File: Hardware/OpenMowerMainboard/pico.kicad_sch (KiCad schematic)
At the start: 7 parts, among them U10 74HC4051, U11 Pico, U7 SN74LV1T34DBV, U9 74HC4051

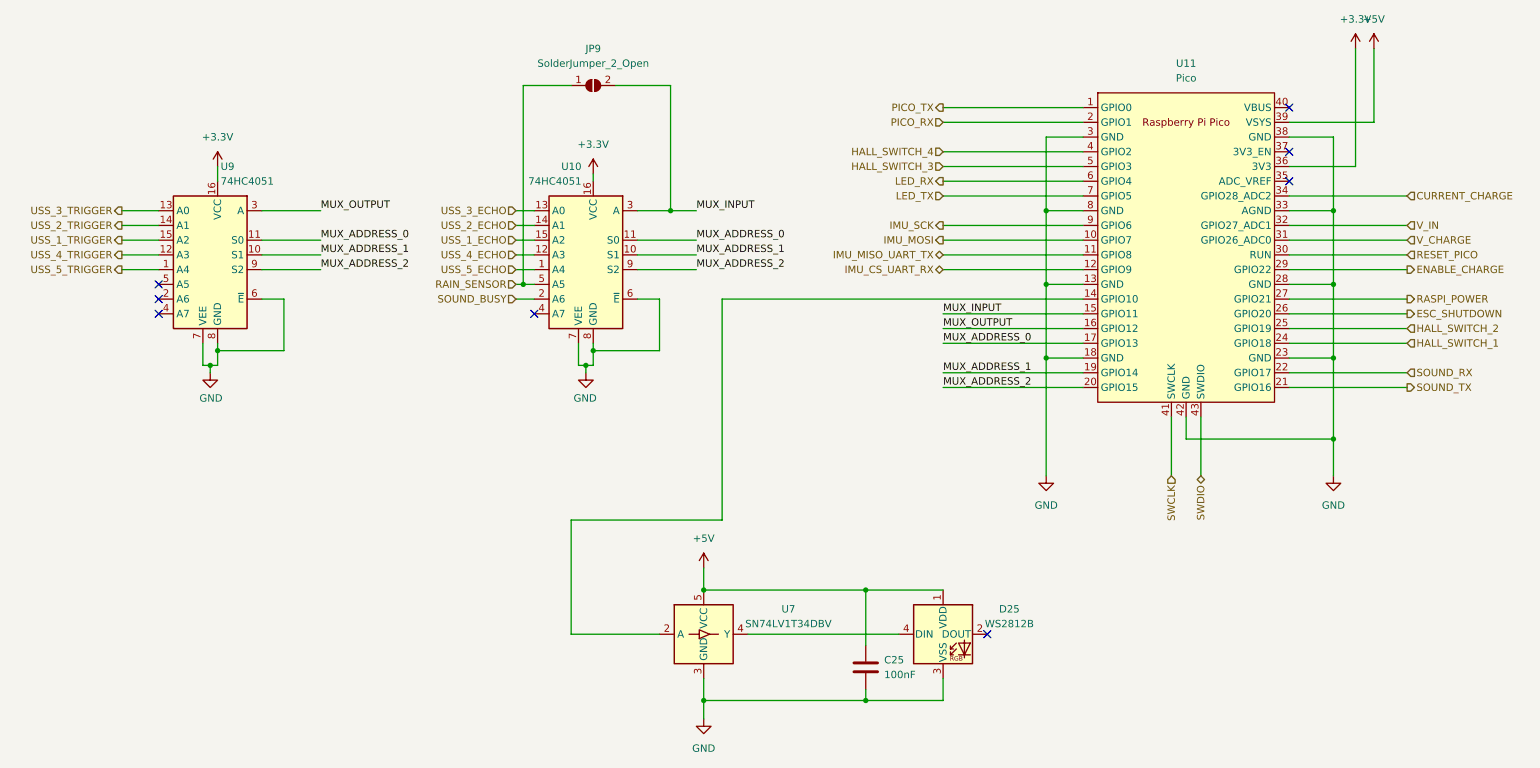
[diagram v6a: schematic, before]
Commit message: feat(Pico/W): update symbol and schematic
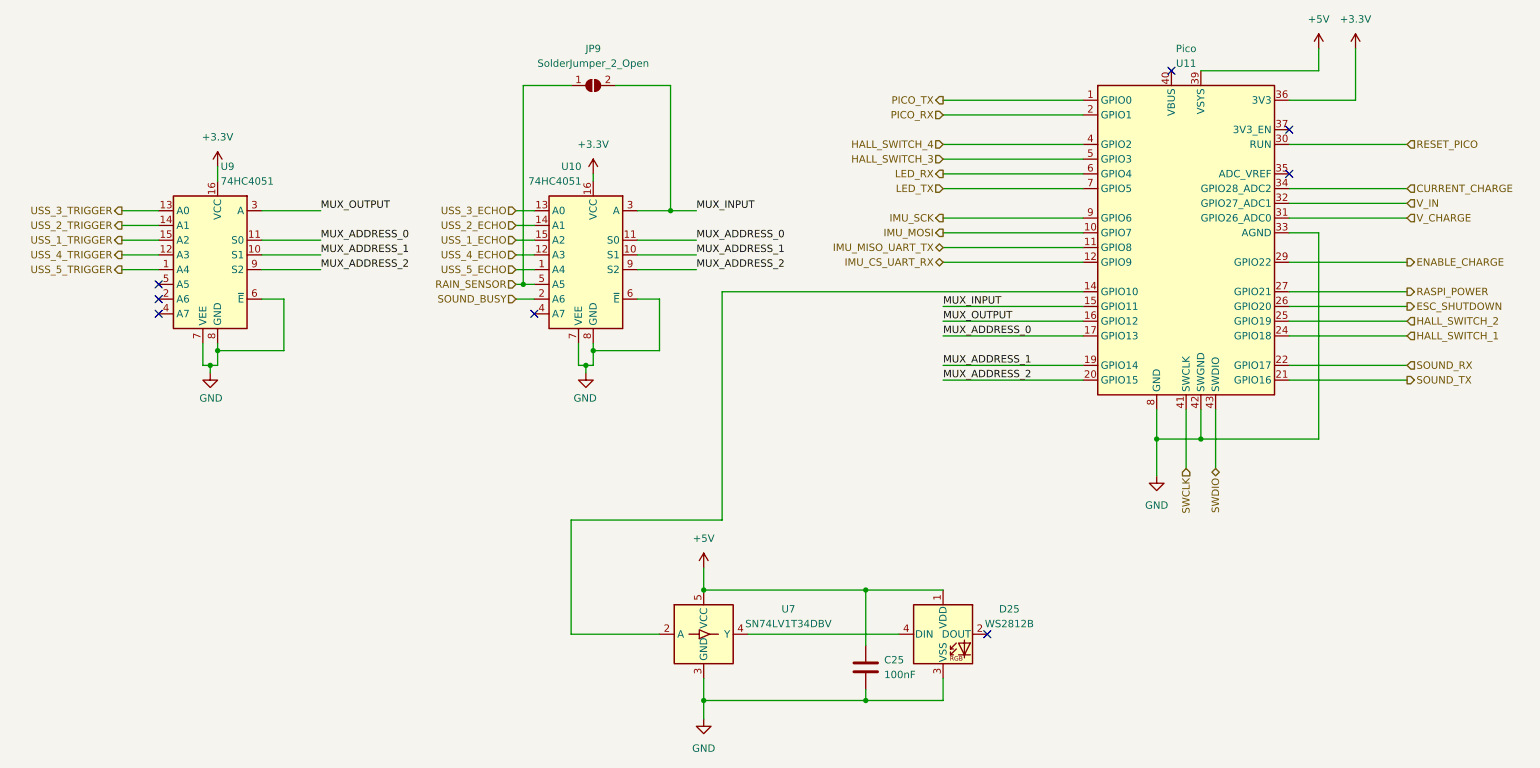
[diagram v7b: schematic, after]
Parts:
- U11: footprint MCU_RaspberryPi_and_Boards:RPi_Pico_SMD_TH -> PicoW:Raspberry_Pi_Pico_SMT_THT; symbol MCU_RaspberryPi_and_Boards:Pico -> PicoW:RaspberryPi-PicoW
